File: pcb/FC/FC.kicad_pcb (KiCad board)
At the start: 4 copper layers, 66 x 71 mm, 96 parts, among them J1 FC-ESC, J2 MIC_1, J3 MIC_2, J4 SCREEN, J5 SERVO, J6 SPEAKER, J7 RC, Q1 DMG3415U, Q2 DMG3415U, SW1 TS-1088-AR02016, SW2 TS-1088-AR02016, SW3 TS-1088-AR02016, U1 STM32F722RETx, U10 XC6206-1.2V_C49446790, U11 MAX98357A, U2 ICM-45686, U4 ESP32-S3-WROOM-1, U5 VL53L1CXV0FY1, U6 LMR51430XDDCR, U7 LMR51430XDDCR, U8 XC6206-2.8V, U9 XC6206P332MR, X1 X322525MOB4SI, X2 Q13FC1350000400

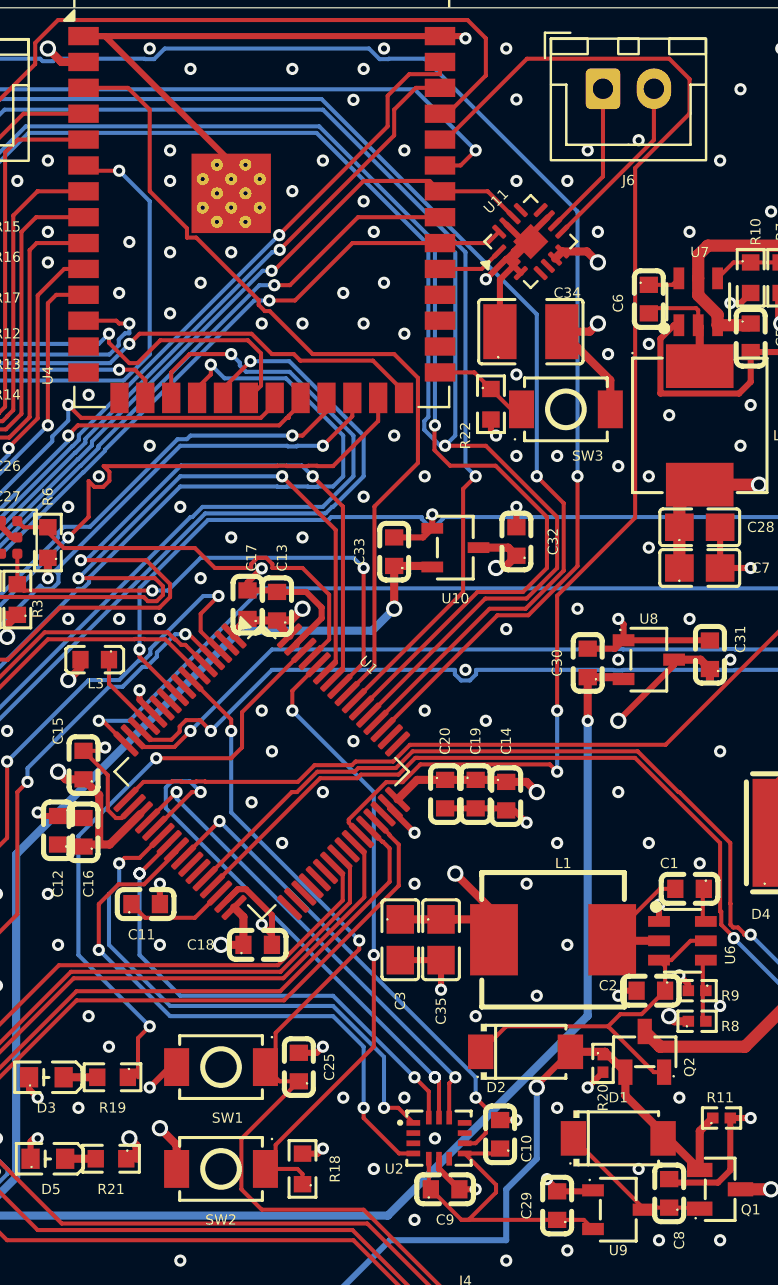
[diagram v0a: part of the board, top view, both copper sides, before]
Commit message: Add companion bring-up, base station features, and PCB updates
Document the verified hardware state and wire protocol, add companion display/audio/camera/telemetry drivers, expand the Python base station and tests, and capture PCB source/manufacturing changes. Stop tracking generated caches and local project state.
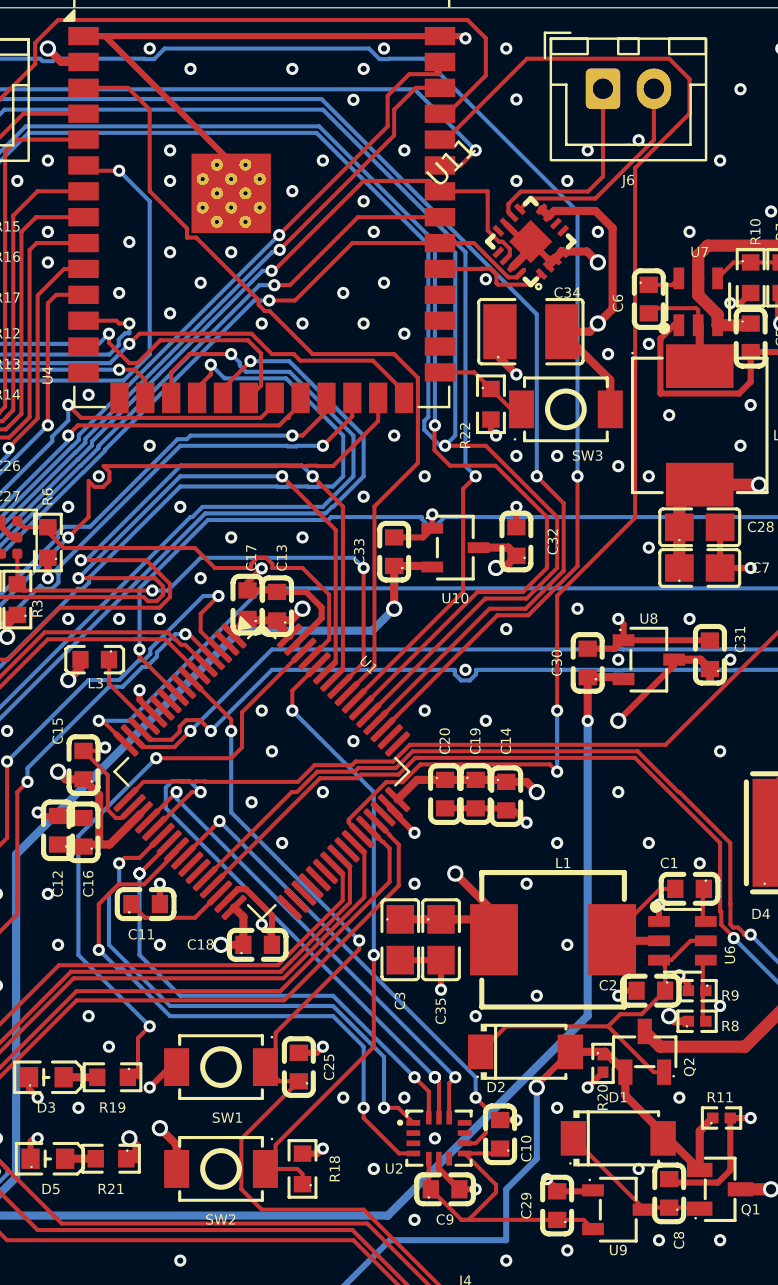
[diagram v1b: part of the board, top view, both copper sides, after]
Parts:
- U11: footprint Package_DFN_QFN:TQFN-16-1EP_3x3mm_P0.5mm_EP1.23x1.23mm -> easyeda2kicad:TQFN-16_L3.0-W3.0-P0.50-BL-EP1.5
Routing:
- net +3.3V: track 91.6 -> 98.7 mm, vias 20 -> 19
- net OUT-: track 7.64 -> 10.2 mm
- net /ESP32/DIN: track 3.26 -> 5.77 mm
- net WS(39): track 91.3 -> 93.5 mm
- net BCLK(38): track 56.7 -> 58.6 mm
- net OUT+: track 8.88 -> 10.5 mm
- net GND: track 185.4 -> 183.9 mm, vias 225 -> 226
